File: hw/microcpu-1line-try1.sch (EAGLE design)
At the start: 52 parts, among them IC1 IC_74HC595-TSSOP-16

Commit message: fixed for microcpu hardware, use fram
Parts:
- added R5: 10K, resistor:R-EU_R0603
- R10, R4, R9: value 10K -> 1K
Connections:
- new net N$5: R5.1, U1.SIO2
- net VCC: now also R5.2
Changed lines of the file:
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@@
 <part name="C11" library="resistor" library_urn="urn:adsk.eagle:library:348" deviceset="C-EU" device="C0603" package3d_urn="urn:adsk.eagle:package:26138/1" value="100nF"/>
 <part name="LED2" library="mouse_enc" deviceset="19-237/R6GHBHC-A04/2T" device=""/>
-<part name="R4" library="resistor" library_urn="urn:adsk.eagle:library:348" deviceset="R-EU_" device="R0603" package3d_urn="urn:adsk.eagle:package:26057/1" value="10K"/>
-<part name="R9" library="resistor" library_urn="urn:adsk.eagle:library:348" deviceset="R-EU_" device="R0603" package3d_urn="urn:adsk.eagle:package:26057/1" value="10K"/>
-<part name="R10" library="resistor" library_urn="urn:adsk.eagle:library:348" deviceset="R-EU_" device="R0603" package3d_urn="urn:adsk.eagle:package:26057/1" value="10K"/>
+<part name="R4" library="resistor" library_urn="urn:adsk.eagle:library:348" deviceset="R-EU_" device="R0603" package3d_urn="urn:adsk.eagle:package:26057/1" value="1K"/>
+<part name="R9" library="resistor" library_urn="urn:adsk.eagle:library:348" deviceset="R-EU_" device="R0603" package3d_urn="urn:adsk.eagle:package:26057/1" value="1K"/>
+<part name="R10" library="resistor" library_urn="urn:adsk.eagle:library:348" deviceset="R-EU_" device="R0603" package3d_urn="urn:adsk.eagle:package:26057/1" value="1K"/>
 <part name="P+12" library="supply1" library_urn="urn:adsk.eagle:library:371" deviceset="VCC" device=""/>
 <part name="JP1" library="pinhead" library_urn="urn:adsk.eagle:library:325" deviceset="PINHD-2X9" device="/90" package3d_urn="urn:adsk.eagle:package:22486/2"/>
@@
 <part name="P+17" library="supply1" library_urn="urn:adsk.eagle:library:371" deviceset="VCC" device=""/>
 <part name="P+18" library="supply1" library_urn="urn:adsk.eagle:library:371" deviceset="VCC" device=""/>
+<part name="R5" library="resistor" library_urn="urn:adsk.eagle:library:348" deviceset="R-EU_" device="R0603" package3d_urn="urn:adsk.eagle:package:26057/1" value="10K"/>
+<part name="P+15" library="supply1" library_urn="urn:adsk.eagle:library:371" deviceset="VCC" device=""/>
 </parts>
 <sheets>
@@
 <instance part="P+18" gate="VCC" x="238.76" y="5.08" smashed="yes">
 <attribute name="VALUE" x="236.22" y="2.54" size="1.778" layer="96" rot="R90"/>
+</instance>
+<instance part="R5" gate="G$1" x="121.92" y="104.14" smashed="yes" rot="R90">
+<attribute name="NAME" x="120.4214" y="100.33" size="1.778" layer="95" rot="R90"/>
+<attribute name="VALUE" x="125.222" y="100.33" size="1.778" layer="96" rot="R90"/>
+</instance>
+<instance part="P+15" gate="VCC" x="121.92" y="114.3" smashed="yes">
+<attribute name="VALUE" x="119.38" y="111.76" size="1.778" layer="96" rot="R90"/>
 </instance>
 </instances>
@@
 <junction x="238.76" y="0"/>
 </segment>
+<segment>
+<pinref part="P+15" gate="VCC" pin="VCC"/>
+<pinref part="R5" gate="G$1" pin="2"/>
+<wire x1="121.92" y1="111.76" x2="121.92" y2="109.22" width="0.1524" layer="91"/>
+</segment>
 </net>
 <net name="TDO" class="0">
@@
 </segment>
 </net>
+<net name="N$5" class="0">
+<segment>
+<pinref part="R5" gate="G$1" pin="1"/>
+<pinref part="U1" gate="G$1" pin="SIO2"/>
+<wire x1="121.92" y1="99.06" x2="121.92" y2="93.98" width="0.1524" layer="91"/>
+<wire x1="121.92" y1="93.98" x2="142.24" y2="93.98" width="0.1524" layer="91"/>
+</segment>
+</net>

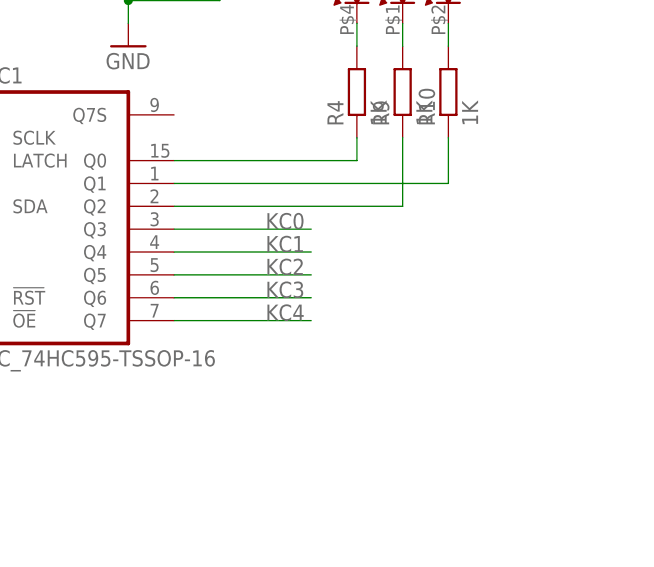
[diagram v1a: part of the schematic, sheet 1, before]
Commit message: wp pullup for fram, diodes for matrix keyboard
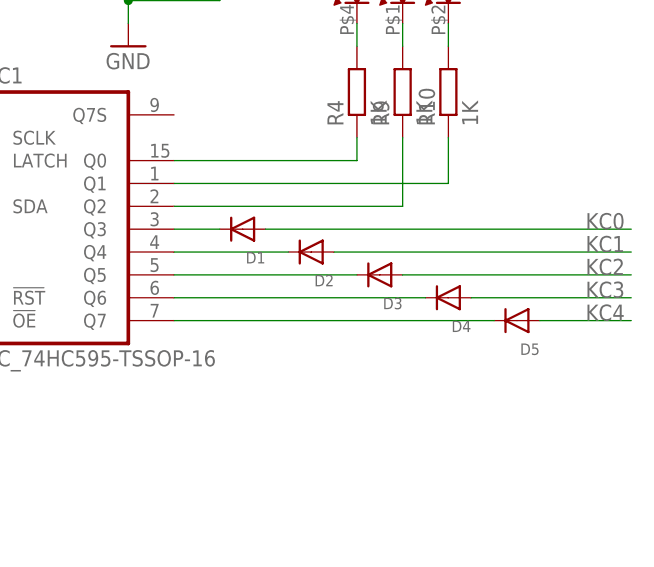
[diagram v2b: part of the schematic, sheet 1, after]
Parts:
- added D1, D2, D3, D4, D5: (no value), adafruit:DIODESOD-123
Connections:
- new net N$13: D1.C, IC1IC.Q3
- new net N$14: D2.C, IC1IC.Q4
- new net N$15: D3.C, IC1IC.Q5
- new net N$16: D4.C, IC1IC.Q6
- new net N$17: D5.C, IC1IC.Q7
- net KC0: now also D1.A; no longer IC1IC.Q3
- net KC1: now also D2.A; no longer IC1IC.Q4
- net KC2: now also D3.A; no longer IC1IC.Q5
- net KC3: now also D4.A; no longer IC1IC.Q6
- net KC4: now also D5.A; no longer IC1IC.Q7
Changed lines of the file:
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@@
 <part name="R5" library="resistor" library_urn="urn:adsk.eagle:library:348" deviceset="R-EU_" device="R0603" package3d_urn="urn:adsk.eagle:package:26057/1" value="10K"/>
 <part name="P+15" library="supply1" library_urn="urn:adsk.eagle:library:371" deviceset="VCC" device=""/>
+<part name="D1" library="adafruit" library_urn="urn:adsk.eagle:library:420" deviceset="DIODE" device="SOD-123"/>
+<part name="D2" library="adafruit" library_urn="urn:adsk.eagle:library:420" deviceset="DIODE" device="SOD-123"/>
+<part name="D3" library="adafruit" library_urn="urn:adsk.eagle:library:420" deviceset="DIODE" device="SOD-123"/>
+<part name="D4" library="adafruit" library_urn="urn:adsk.eagle:library:420" deviceset="DIODE" device="SOD-123"/>
+<part name="D5" library="adafruit" library_urn="urn:adsk.eagle:library:420" deviceset="DIODE" device="SOD-123"/>
 </parts>
 <sheets>
@@
 <instance part="P+15" gate="VCC" x="121.92" y="114.3" smashed="yes">
 <attribute name="VALUE" x="119.38" y="111.76" size="1.778" layer="96" rot="R90"/>
+</instance>
+<instance part="D1" gate="G$1" x="238.76" y="66.04" smashed="yes" rot="R180">
+<attribute name="NAME" x="241.3" y="63.5" size="1.27" layer="95" rot="R180"/>
+<attribute name="VALUE" x="241.3" y="69.85" size="1.27" layer="96" rot="R180"/>
+</instance>
+<instance part="D2" gate="G$1" x="246.38" y="63.5" smashed="yes" rot="R180">
+<attribute name="NAME" x="248.92" y="60.96" size="1.27" layer="95" rot="R180"/>
+<attribute name="VALUE" x="248.92" y="67.31" size="1.27" layer="96" rot="R180"/>
+</instance>
+<instance part="D3" gate="G$1" x="254" y="60.96" smashed="yes" rot="R180">
+<attribute name="NAME" x="256.54" y="58.42" size="1.27" layer="95" rot="R180"/>
+<attribute name="VALUE" x="256.54" y="64.77" size="1.27" layer="96" rot="R180"/>
+</instance>
+<instance part="D4" gate="G$1" x="261.62" y="58.42" smashed="yes" rot="R180">
+<attribute name="NAME" x="264.16" y="55.88" size="1.27" layer="95" rot="R180"/>
+<attribute name="VALUE" x="264.16" y="62.23" size="1.27" layer="96" rot="R180"/>
+</instance>
+<instance part="D5" gate="G$1" x="269.24" y="55.88" smashed="yes" rot="R180">
+<attribute name="NAME" x="271.78" y="53.34" size="1.27" layer="95" rot="R180"/>
+<attribute name="VALUE" x="271.78" y="59.69" size="1.27" layer="96" rot="R180"/>
 </instance>
 </instances>
@@
 </segment>
 </net>
-<net name="KC4" class="0">
-<segment>
-<pinref part="IC1" gate="IC" pin="Q7"/>
-<wire x1="231.14" y1="55.88" x2="246.38" y2="55.88" width="0.1524" layer="91"/>
-<label x="241.3" y="55.88" size="1.778" layer="95"/>
-</segment>
-</net>
-<net name="KC3" class="0">
-<segment>
-<pinref part="IC1" gate="IC" pin="Q6"/>
-<wire x1="231.14" y1="58.42" x2="246.38" y2="58.42" width="0.1524" layer="91"/>
-<label x="241.3" y="58.42" size="1.778" layer="95"/>
-</segment>
-</net>
-<net name="KC2" class="0">
-<segment>
-<pinref part="IC1" gate="IC" pin="Q5"/>
-<wire x1="231.14" y1="60.96" x2="246.38" y2="60.96" width="0.1524" layer="91"/>
-<label x="241.3" y="60.96" size="1.778" layer="95"/>
-</segment>
-</net>
-<net name="KC1" class="0">
-<segment>
-<pinref part="IC1" gate="IC" pin="Q4"/>
-<wire x1="231.14" y1="63.5" x2="246.38" y2="63.5" width="0.1524" layer="91"/>
-<label x="241.3" y="63.5" size="1.778" layer="95"/>
-</segment>
-</net>
-<net name="KC0" class="0">
-<segment>
-<pinref part="IC1" gate="IC" pin="Q3"/>
-<wire x1="231.14" y1="66.04" x2="246.38" y2="66.04" width="0.1524" layer="91"/>
-<label x="241.3" y="66.04" size="1.778" layer="95"/>
-</segment>
-</net>
 <net name="REG_LATCH" class="0">
 <segment>
@@
 <wire x1="121.92" y1="99.06" x2="121.92" y2="93.98" width="0.1524" layer="91"/>
 <wire x1="121.92" y1="93.98" x2="142.24" y2="93.98" width="0.1524" layer="91"/>
+</segment>
+</net>
+<net name="N$13" class="0">
+<segment>
+<pinref part="IC1" gate="IC" pin="Q3"/>
+<pinref part="D1" gate="G$1" pin="C"/>
+<wire x1="231.14" y1="66.04" x2="236.22" y2="66.04" width="0.1524" layer="91"/>
+</segment>
+</net>
+<net name="N$14" class="0">
+<segment>
+<pinref part="IC1" gate="IC" pin="Q4"/>
+<pinref part="D2" gate="G$1" pin="C"/>
+<wire x1="231.14" y1="63.5" x2="243.84" y2="63.5" width="0.1524" layer="91"/>
+</segment>
+</net>
+<net name="N$15" class="0">
+<segment>
+<pinref part="IC1" gate="IC" pin="Q5"/>
+<pinref part="D3" gate="G$1" pin="C"/>
+<wire x1="231.14" y1="60.96" x2="251.46" y2="60.96" width="0.1524" layer="91"/>
+</segment>
+</net>
+<net name="N$16" class="0">
+<segment>
+<pinref part="IC1" gate="IC" pin="Q6"/>
+<pinref part="D4" gate="G$1" pin="C"/>
+<wire x1="231.14" y1="58.42" x2="259.08" y2="58.42" width="0.1524" layer="91"/>
+</segment>
+</net>
+<net name="N$17" class="0">
+<segment>
+<pinref part="IC1" gate="IC" pin="Q7"/>
+<pinref part="D5" gate="G$1" pin="C"/>
+<wire x1="231.14" y1="55.88" x2="266.7" y2="55.88" width="0.1524" layer="91"/>
+</segment>
+</net>
+<net name="KC0" class="0">
+<segment>
+<pinref part="D1" gate="G$1" pin="A"/>
+<wire x1="241.3" y1="66.04" x2="281.94" y2="66.04" width="0.1524" layer="91"/>
+<label x="276.86" y="66.04" size="1.778" layer="95"/>
+</segment>
+</net>
+<net name="KC1" class="0">
+<segment>
+<pinref part="D2" gate="G$1" pin="A"/>
+<wire x1="248.92" y1="63.5" x2="281.94" y2="63.5" width="0.1524" layer="91"/>
+<label x="276.86" y="63.5" size="1.778" layer="95"/>
+</segment>
+</net>
+<net name="KC2" class="0">
+<segment>
+<pinref part="D3" gate="G$1" pin="A"/>
+<wire x1="256.54" y1="60.96" x2="281.94" y2="60.96" width="0.1524" layer="91"/>
+<label x="276.86" y="60.96" size="1.778" layer="95"/>
+</segment>
+</net>
+<net name="KC3" class="0">
+<segment>
+<pinref part="D4" gate="G$1" pin="A"/>
+<wire x1="264.16" y1="58.42" x2="281.94" y2="58.42" width="0.1524" layer="91"/>
+<label x="276.86" y="58.42" size="1.778" layer="95"/>
+</segment>
+</net>
+<net name="KC4" class="0">
+<segment>
+<pinref part="D5" gate="G$1" pin="A"/>
+<wire x1="271.78" y1="55.88" x2="281.94" y2="55.88" width="0.1524" layer="91"/>
+<label x="276.86" y="55.88" size="1.778" layer="95"/>
 </segment>
 </net>
@@
 <junction x="129.54" y="7.62"/>
 <junction x="152.4" y="-2.54"/>
-<wire x1="152.4" y1="-2.54" x2="172.72" y2="-2.54" width="0.1524" layer="91"/>
-<label x="167.64" y="-2.54" size="1.778" layer="95"/>
+<wire x1="152.4" y1="-5.08" x2="177.8" y2="-5.08" width="0.1524" layer="91"/>
+<junction x="152.4" y="-5.08"/>
+<label x="172.72" y="-5.08" size="1.778" layer="95"/>
 </segment>
 </net>
@@
 <junction x="129.54" y="-10.16"/>
 <junction x="152.4" y="-20.32"/>
-<wire x1="152.4" y1="-20.32" x2="172.72" y2="-20.32" width="0.1524" layer="91"/>
-<label x="167.64" y="-20.32" size="1.778" layer="95"/>
+<wire x1="152.4" y1="-22.86" x2="177.8" y2="-22.86" width="0.1524" layer="91"/>
+<junction x="152.4" y="-22.86"/>
+<label x="172.72" y="-22.86" size="1.778" layer="95"/>
 </segment>
 </net>
@@
 <junction x="106.68" y="-38.1"/>
 <junction x="106.68" y="-27.94"/>
-<wire x1="152.4" y1="-38.1" x2="172.72" y2="-38.1" width="0.1524" layer="91"/>
-<label x="167.64" y="-38.1" size="1.778" layer="95"/>
+<wire x1="152.4" y1="-40.64" x2="177.8" y2="-40.64" width="0.1524" layer="91"/>
+<junction x="152.4" y="-40.64"/>
+<label x="172.72" y="-40.64" size="1.778" layer="95"/>
 </segment>
 </net>
@@
 <junction x="129.54" y="-45.72"/>
 <wire x1="152.4" y1="-58.42" x2="152.4" y2="-55.88" width="0.1524" layer="91"/>
-<wire x1="152.4" y1="-55.88" x2="172.72" y2="-55.88" width="0.1524" layer="91"/>
-<label x="167.64" y="-55.88" size="1.778" layer="95"/>
+<junction x="152.4" y="-58.42"/>
+<wire x1="165.1" y1="-58.42" x2="167.64" y2="-58.42" width="0.1524" layer="91"/>
+<label x="172.72" y="-58.42" size="1.778" layer="95"/>
+<wire x1="167.64" y1="-58.42" x2="177.8" y2="-58.42" width="0.1524" layer="91"/>
+<wire x1="152.4" y1="-58.42" x2="165.1" y2="-58.42" width="0.1524" layer="91"/>
 </segment>
 </net>
@@
 <junction x="106.68" y="-73.66"/>
 <junction x="106.68" y="-63.5"/>
-<wire x1="152.4" y1="-73.66" x2="172.72" y2="-73.66" width="0.1524" layer="91"/>
-<label x="167.64" y="-73.66" size="1.778" layer="95"/>
-</segment>
-</net>
+<wire x1="152.4" y1="-76.2" x2="177.8" y2="-76.2" width="0.1524" layer="91"/>
+<junction x="152.4" y="-76.2"/>
+<label x="172.72" y="-76.2" size="1.778" layer="95"/>
+</segment>
+</net>
